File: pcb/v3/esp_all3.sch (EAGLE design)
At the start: 25 parts, among them Q1 BUZ11BH

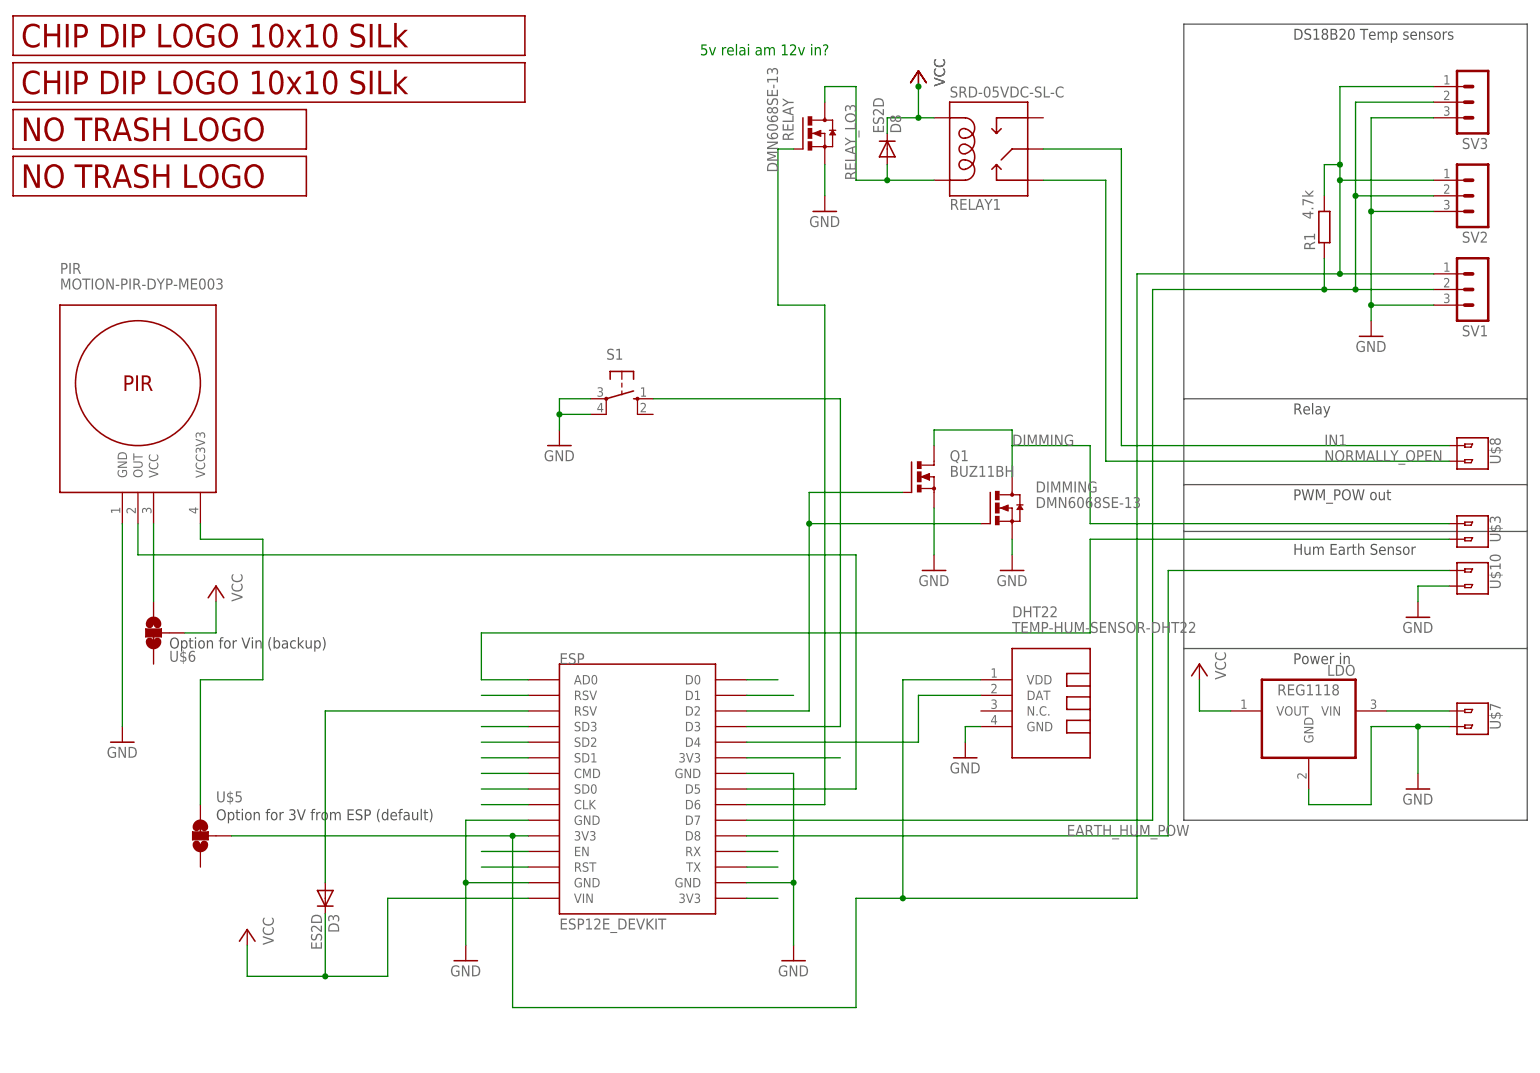
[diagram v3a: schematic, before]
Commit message: flipped PIR
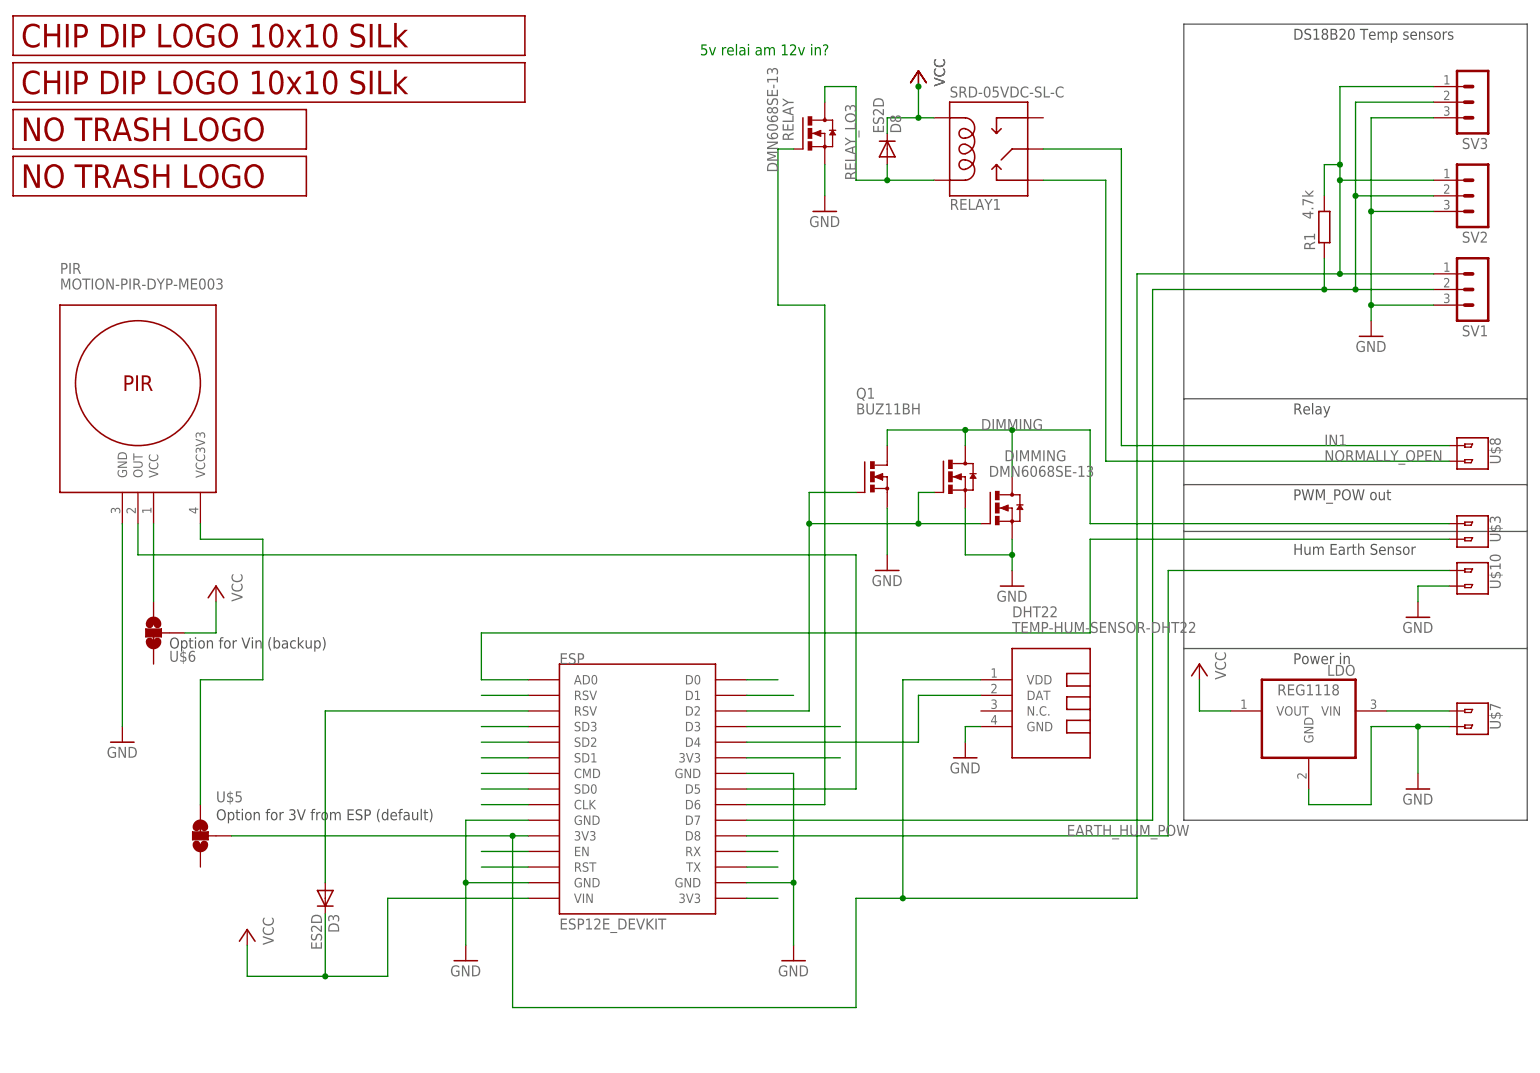
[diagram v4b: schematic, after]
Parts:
- removed S1: (no value), switch-omron:40/XX
- added DIMMING2: DMN6068SE-13, transistor-power:NMOSFET_SMD_223
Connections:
- net DIMMING: now also DIMMING2.D
- net GND: now also DIMMING2.S; no longer S1.P, S1.P1
- net N$27: no longer S1.S
- net TTL_DIMM: now also DIMMING2.G
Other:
- moved on the sheet: Q1
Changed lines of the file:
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@@
 <?xml version="1.0" encoding="utf-8"?>
 <!DOCTYPE eagle SYSTEM "eagle.dtd">
-<eagle version="7.6.0">
+<eagle version="7.7.0">
 <drawing>
 <settings>
@@
 <part name="GND7" library="supply1" deviceset="GND" device=""/>
 <part name="GND9" library="supply1" deviceset="GND" device=""/>
-<part name="S1" library="switch-omron" deviceset="40/XX" device=""/>
-<part name="GND10" library="supply1" deviceset="GND" device=""/>
 <part name="U$1" library="JKW_CHIP" deviceset="LOGO_10X10_SILK" device=""/>
 <part name="U$4" library="JKW_CHIP" deviceset="LOGO_NO_TRASH" device="NO_TRASH"/>
@@
 <part name="Q1" library="transistor-power" deviceset="BUZ11" device="BH"/>
 <part name="GND11" library="supply1" deviceset="GND" device=""/>
+<part name="DIMMING2" library="transistor-power" deviceset="NMOSFET_SMD_223" device="" value="DMN6068SE-13"/>
 </parts>
 <sheets>
@@
 <attribute name="NAME" x="216.662" y="85.852" size="1.778" layer="95" rot="R90"/>
 </instance>
-<instance part="DIMMING" gate="G$1" x="134.62" y="91.44"/>
-<instance part="GND3" gate="1" x="137.16" y="81.28"/>
+<instance part="DIMMING" gate="G$1" x="134.62" y="91.44" smashed="yes">
+<attribute name="NAME" x="135.89" y="99.06" size="1.778" layer="95"/>
+<attribute name="VALUE" x="133.35" y="96.52" size="1.778" layer="96"/>
+</instance>
+<instance part="GND3" gate="1" x="137.16" y="78.74"/>
 <instance part="U$5" gate="G$1" x="5.08" y="38.1" smashed="yes" rot="MR0">
 <attribute name="NAME" x="7.62" y="43.561" size="1.778" layer="95"/>
@@
 <instance part="GND7" gate="1" x="195.58" y="119.38"/>
 <instance part="GND9" gate="1" x="129.54" y="50.8"/>
-<instance part="S1" gate="1" x="73.66" y="109.22" rot="R270"/>
-<instance part="GND10" gate="1" x="63.5" y="101.6"/>
 <instance part="U$1" gate="G$1" x="-25.4" y="165.1"/>
 <instance part="U$4" gate="G$1" x="-25.4" y="142.24"/>
@@
 <instance part="D3" gate="G$1" x="25.4" y="27.94" rot="R270"/>
 <instance part="LDO" gate="G$1" x="185.42" y="58.42" rot="MR0"/>
-<instance part="Q1" gate="1" x="121.92" y="96.52"/>
-<instance part="GND11" gate="1" x="124.46" y="81.28"/>
+<instance part="Q1" gate="1" x="114.3" y="96.52" smashed="yes">
+<attribute name="NAME" x="111.76" y="109.22" size="1.778" layer="95"/>
+<attribute name="VALUE" x="111.76" y="106.68" size="1.778" layer="96"/>
+</instance>
+<instance part="GND11" gate="1" x="116.84" y="81.28"/>
+<instance part="DIMMING2" gate="G$1" x="127" y="96.52" smashed="yes"/>
 </instances>
 <busses>
@@
 <pinref part="ESP" gate="G$1" pin="D3"/>
 <wire x1="93.98" y1="55.88" x2="109.22" y2="55.88" width="0.1524" layer="91"/>
-<wire x1="109.22" y1="55.88" x2="109.22" y2="109.22" width="0.1524" layer="91"/>
-<pinref part="S1" gate="1" pin="S"/>
-<wire x1="109.22" y1="109.22" x2="78.74" y2="109.22" width="0.1524" layer="91"/>
 </segment>
 </net>
@@
 <wire x1="104.14" y1="58.42" x2="104.14" y2="88.9" width="0.1524" layer="91"/>
 <pinref part="DIMMING" gate="G$1" pin="G"/>
-<wire x1="132.08" y1="88.9" x2="104.14" y2="88.9" width="0.1524" layer="91"/>
+<wire x1="132.08" y1="88.9" x2="121.92" y2="88.9" width="0.1524" layer="91"/>
 <pinref part="Q1" gate="1" pin="G"/>
-<wire x1="119.38" y1="93.98" x2="104.14" y2="93.98" width="0.1524" layer="91"/>
+<wire x1="121.92" y1="88.9" x2="104.14" y2="88.9" width="0.1524" layer="91"/>
+<wire x1="111.76" y1="93.98" x2="104.14" y2="93.98" width="0.1524" layer="91"/>
 <wire x1="104.14" y1="93.98" x2="104.14" y2="88.9" width="0.1524" layer="91"/>
 <junction x="104.14" y="88.9"/>
+<pinref part="DIMMING2" gate="G$1" pin="G"/>
+<wire x1="124.46" y1="93.98" x2="121.92" y2="93.98" width="0.1524" layer="91"/>
+<wire x1="121.92" y1="93.98" x2="121.92" y2="88.9" width="0.1524" layer="91"/>
+<junction x="121.92" y="88.9"/>
 </segment>
 </net>
@@
 <pinref part="DIMMING" gate="G$1" pin="S"/>
 <pinref part="GND3" gate="1" pin="GND"/>
+<wire x1="137.16" y1="81.28" x2="137.16" y2="83.82" width="0.1524" layer="91"/>
+<pinref part="DIMMING2" gate="G$1" pin="S"/>
 <wire x1="137.16" y1="83.82" x2="137.16" y2="86.36" width="0.1524" layer="91"/>
+<wire x1="129.54" y1="91.44" x2="129.54" y2="83.82" width="0.1524" layer="91"/>
+<wire x1="129.54" y1="83.82" x2="137.16" y2="83.82" width="0.1524" layer="91"/>
+<junction x="137.16" y="83.82"/>
 </segment>
 <segment>
@@
 </segment>
 <segment>
-<pinref part="S1" gate="1" pin="P1"/>
-<pinref part="GND10" gate="1" pin="GND"/>
-<wire x1="68.58" y1="106.68" x2="63.5" y2="106.68" width="0.1524" layer="91"/>
-<wire x1="63.5" y1="106.68" x2="63.5" y2="104.14" width="0.1524" layer="91"/>
-<pinref part="S1" gate="1" pin="P"/>
-<wire x1="68.58" y1="109.22" x2="63.5" y2="109.22" width="0.1524" layer="91"/>
-<wire x1="63.5" y1="109.22" x2="63.5" y2="106.68" width="0.1524" layer="91"/>
-<junction x="63.5" y="106.68"/>
-</segment>
-<segment>
 <pinref part="Q1" gate="1" pin="S"/>
 <pinref part="GND11" gate="1" pin="GND"/>
-<wire x1="124.46" y1="91.44" x2="124.46" y2="83.82" width="0.1524" layer="91"/>
+<wire x1="116.84" y1="91.44" x2="116.84" y2="83.82" width="0.1524" layer="91"/>
 </segment>
 </net>
@@
 <segment>
 <pinref part="DIMMING" gate="G$1" pin="D"/>
-<wire x1="137.16" y1="96.52" x2="137.16" y2="101.6" width="0.1524" layer="91"/>
-<wire x1="137.16" y1="101.6" x2="149.86" y2="101.6" width="0.1524" layer="91"/>
-<wire x1="149.86" y1="101.6" x2="149.86" y2="88.9" width="0.1524" layer="91"/>
+<wire x1="137.16" y1="96.52" x2="137.16" y2="104.14" width="0.1524" layer="91"/>
+<wire x1="137.16" y1="104.14" x2="149.86" y2="104.14" width="0.1524" layer="91"/>
+<wire x1="149.86" y1="104.14" x2="149.86" y2="88.9" width="0.1524" layer="91"/>
 <pinref part="U$3" gate="G$1" pin="1"/>
 <wire x1="149.86" y1="88.9" x2="208.28" y2="88.9" width="0.1524" layer="91"/>
-<label x="137.16" y="101.6" size="1.778" layer="95"/>
-<wire x1="137.16" y1="101.6" x2="137.16" y2="104.14" width="0.1524" layer="91"/>
-<wire x1="137.16" y1="104.14" x2="124.46" y2="104.14" width="0.1524" layer="91"/>
+<label x="132.08" y="104.14" size="1.778" layer="95"/>
+<wire x1="137.16" y1="104.14" x2="129.54" y2="104.14" width="0.1524" layer="91"/>
 <pinref part="Q1" gate="1" pin="D"/>
-<wire x1="124.46" y1="104.14" x2="124.46" y2="101.6" width="0.1524" layer="91"/>
-</segment>
-</net>
+<wire x1="129.54" y1="104.14" x2="116.84" y2="104.14" width="0.1524" layer="91"/>
+<wire x1="116.84" y1="104.14" x2="116.84" y2="101.6" width="0.1524" layer="91"/>
+<pinref part="DIMMING2" gate="G$1" pin="D"/>
+<wire x1="129.54" y1="101.6" x2="129.54" y2="104.14" width="0.1524" layer="91"/>
+<junction x="129.54" y="104.14"/>
+<junction x="137.16" y="104.14"/>
+</segment>
+</net>

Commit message: added more transistors
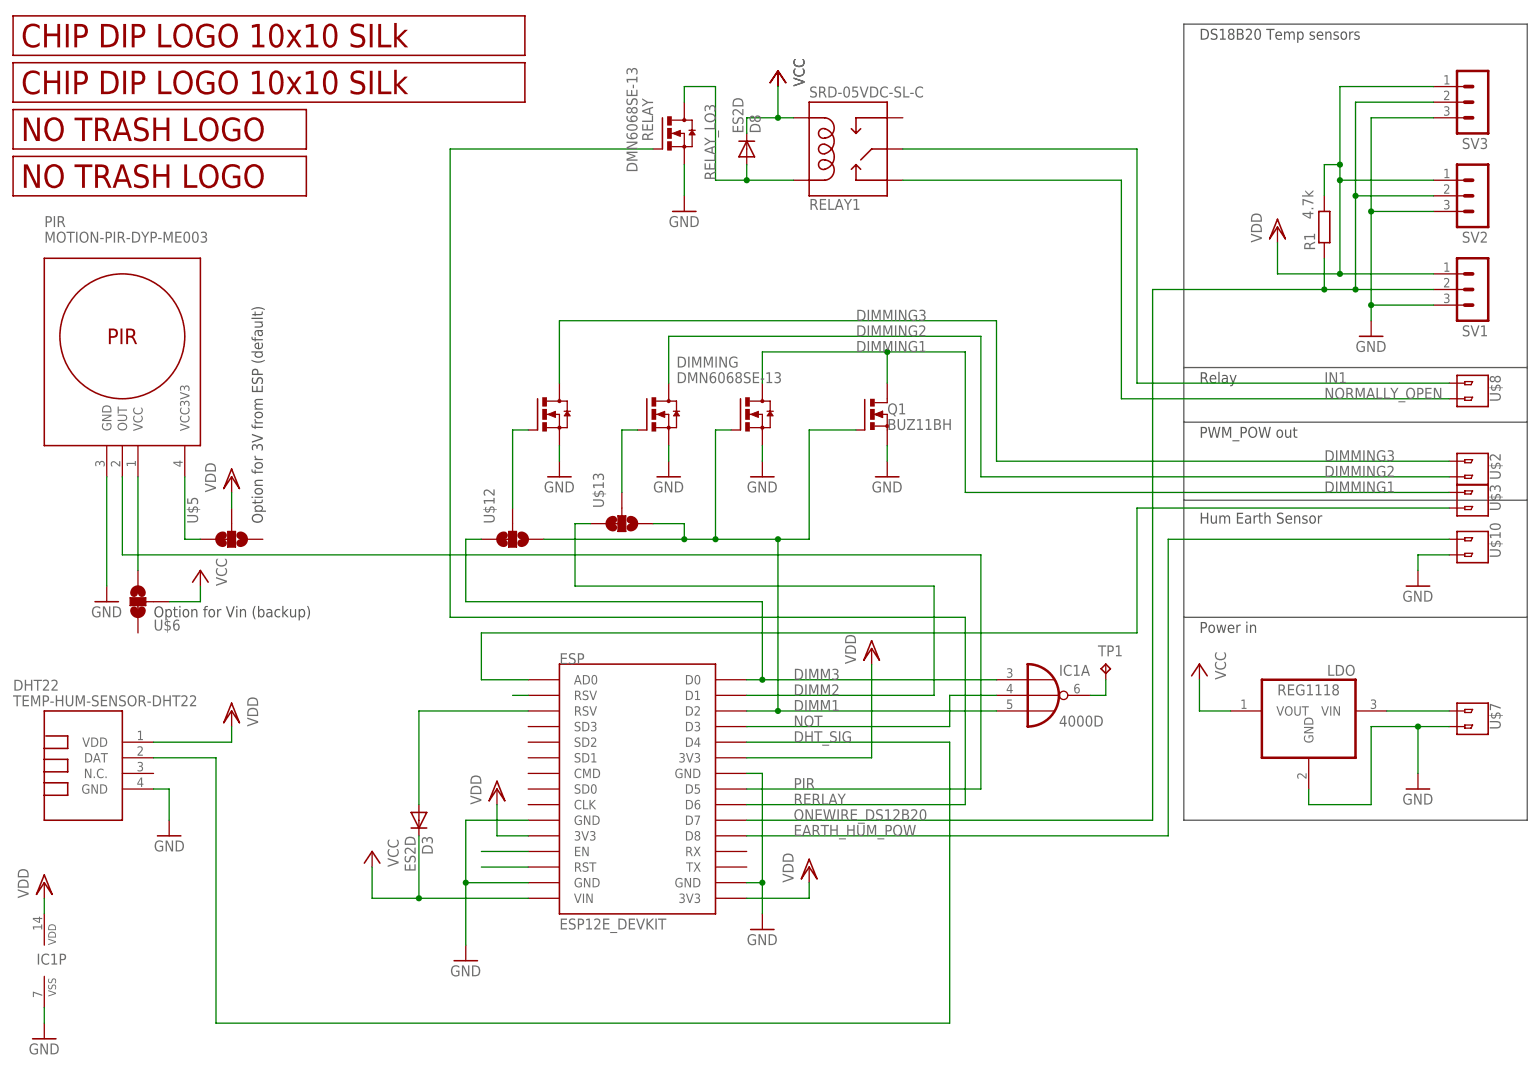
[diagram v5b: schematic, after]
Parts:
- added DIMMING1: DMN6068SE-13, transistor-power:NMOSFET_SMD_223
- added IC1: 4000D, 40xx:4000D
- added TP1: TPTP20SQ, testpad:TPTP20SQ
- added U$12, U$13: SMD_SJ_3WAY_CLOSED, JKW_CHIP:SMD_SJ_3WAY_CLOSED
- added U$2: V1, JKW_CHIP:2_PIN_CONNECTOR
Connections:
- net N$10 renamed RERLAY
- net N$15 renamed ONEWIRE_DS12B20
- removed net 3V3: DHT22.VDD, ESP.3V3@0, R1.2, SV1.1, SV2.1, SV3.1, U$5.2
- removed net DIMMING: DIMMING.D, DIMMING2.D, Q1.D, U$3.1
- removed net N$11: ESP.3V3@2
- removed net N$16: ESP.D1
- removed net N$18: ESP.TX
- removed net N$19: ESP.RX
- removed net N$27: ESP.D3
- removed net N$3: ESP.3V3@1
- removed net N$30: ESP.D0
- removed net N$5: ESP.SD2
- removed net N$6: ESP.SD1
- removed net N$7: ESP.CMD
- removed net N$8: ESP.SD0
- removed net N$9: ESP.CLK
- removed net TTL_DIMM: DIMMING.G, DIMMING2.G, ESP.D2, Q1.G
- new net DIMM1: DIMMING.G, ESP.D2, IC1A.I2, Q1.G, U$12.3, U$13.3
- new net DIMM2: ESP.D1, U$13.1
- new net DIMM3: ESP.D0, IC1A.I0, U$12.1
- new net DIMMING1: DIMMING.D, Q1.D, U$3.1
- new net DIMMING2: DIMMING1.D, U$2.2
- new net DIMMING3: DIMMING2.D, U$2.1
- new net N$20: DIMMING2.G, U$12.2
- new net N$21: DIMMING1.G, U$13.2
- new net NOT: ESP.D3, IC1A.I1
- new net VDD: DHT22.VDD, ESP.3V3@0, ESP.3V3@1, ESP.3V3@2, IC1P.VDD, R1.2, SV1.1, SV2.1, SV3.1, U$5.2
- net GND: now also DIMMING1.S, IC1P.VSS
- net N$4: now also IC1A.O, TP1.TP; no longer ESP.SD3
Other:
- note removed: "5v relai am 12v in?"
- moved on the sheet: D3, D8, DHT22, DIMMING, PIR, Q1, RELAY, RELAY1, U$10, U$3, U$5, U$6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
